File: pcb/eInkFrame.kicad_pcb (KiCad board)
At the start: 2 copper layers, 191.8 x 127.7 mm, 22 parts, among them J1 Socket Raspberry, J2 Socket IT8951, J3 Socket BME680, J40 Socket MPR121 comm, J41 Socket MPR121 contacts, U1 Raspberry, U2 IT8951_Driver, U3 CJMCU-680, U4 MPR121

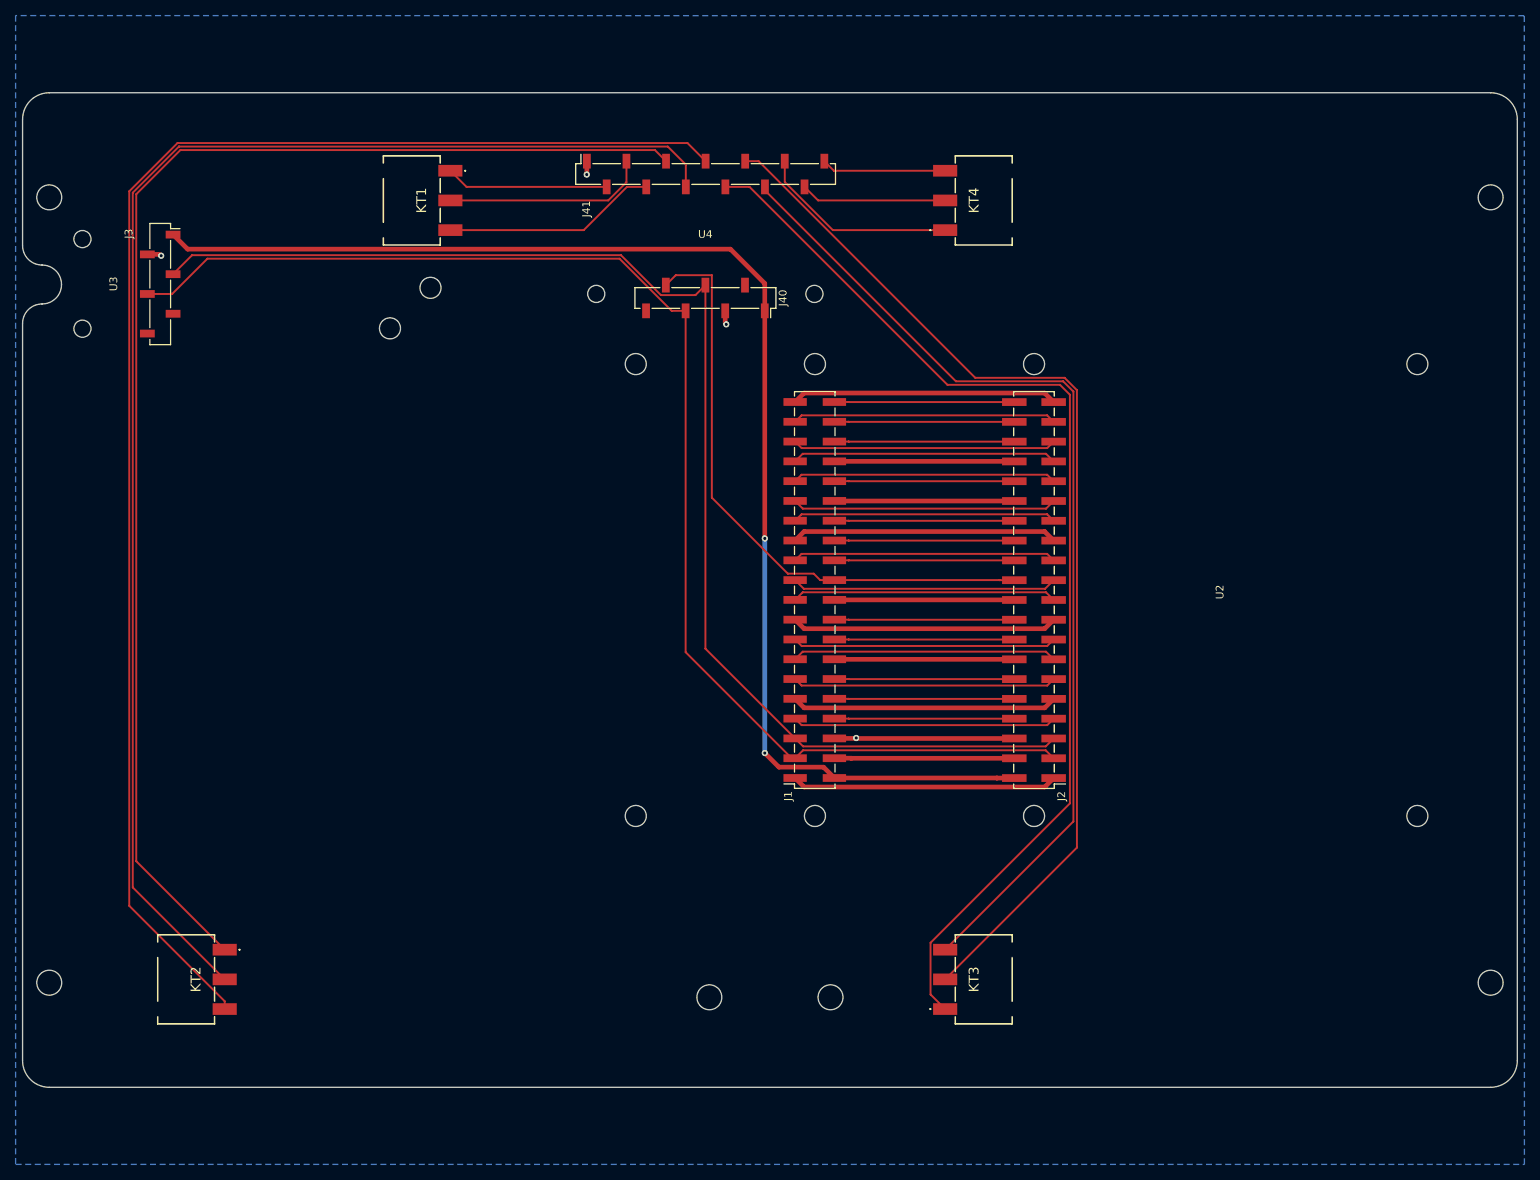
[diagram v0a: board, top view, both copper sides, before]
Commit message: Global doc cleanup, pcb and scripts enhancement, adding images
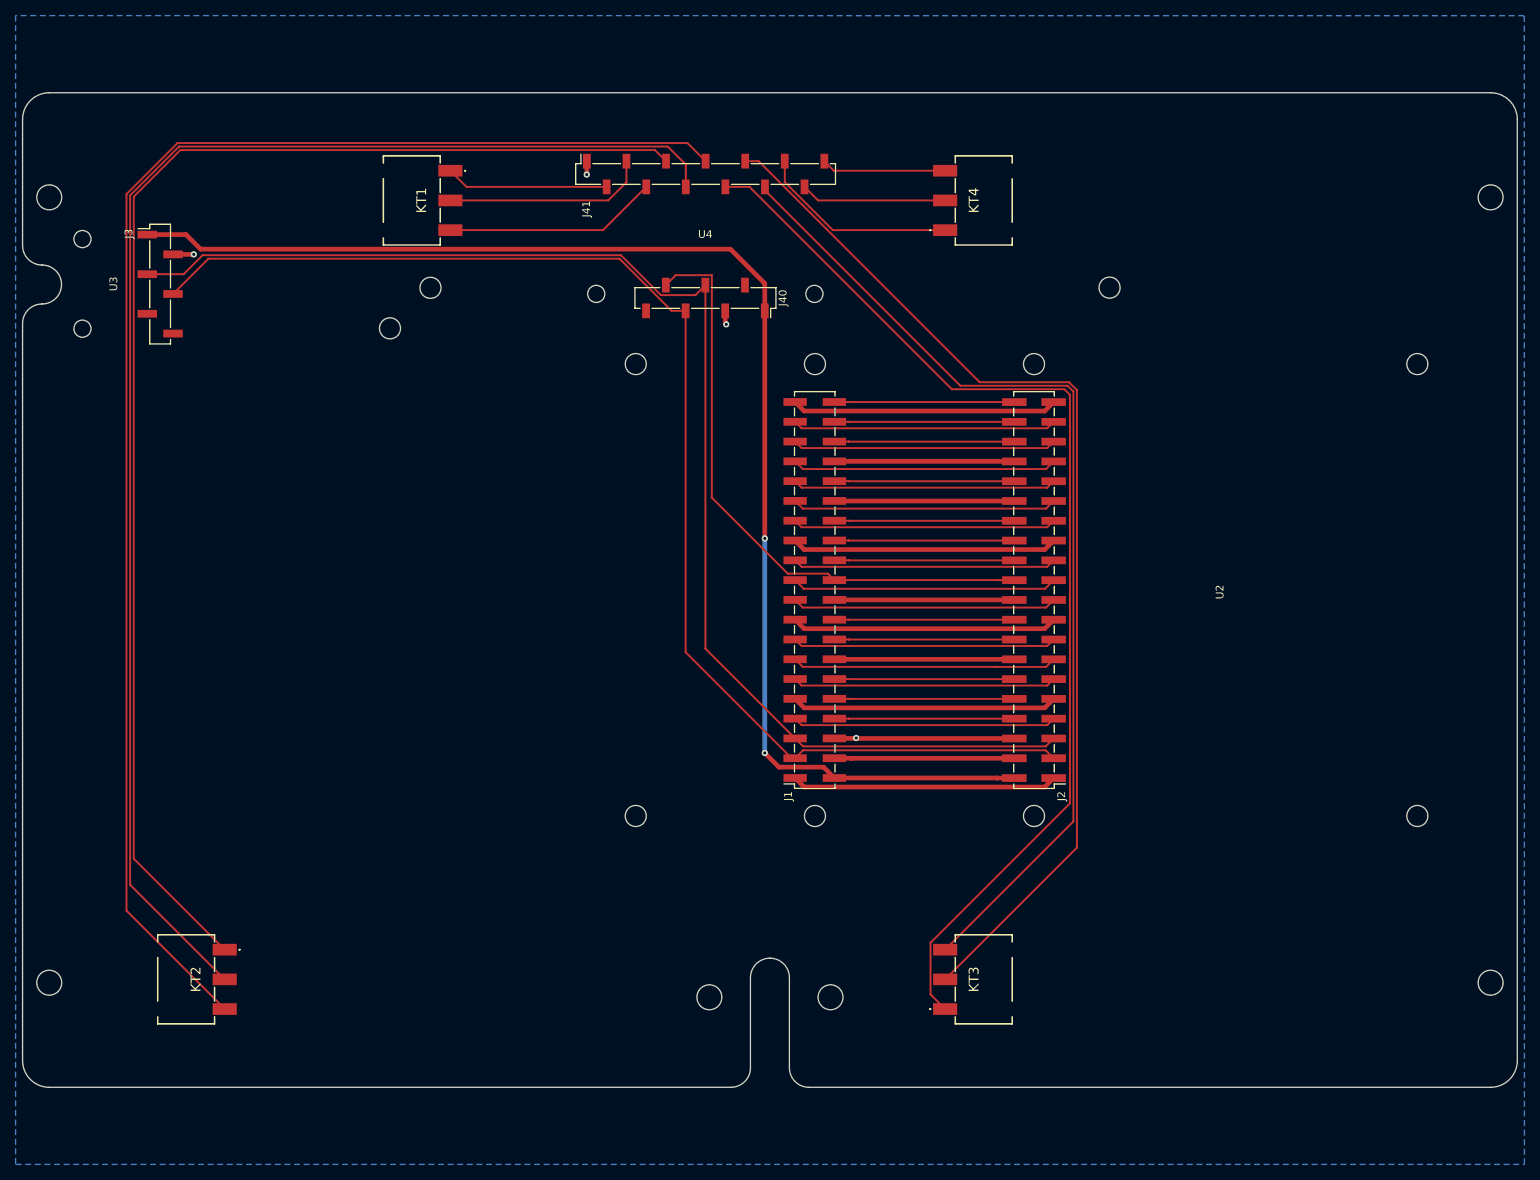
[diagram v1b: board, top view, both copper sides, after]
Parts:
- added HF3: M2.5, MountingHole:MountingHole_2.7mm_M2.5, F.Cu at (155.8, 50.9)
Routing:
- net VIN: track 172.2 -> 175.5 mm
- net SCL: track 169.0 -> 172.3 mm
- net SDA: track 171.3 -> 168.0 mm
- net GND: track 28.3 -> 29.3 mm
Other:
- outline, holes or cut-outs redrawn

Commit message: Change a hard to source component and adapt PCB accordingly + hide some Spotify elements + global formatting
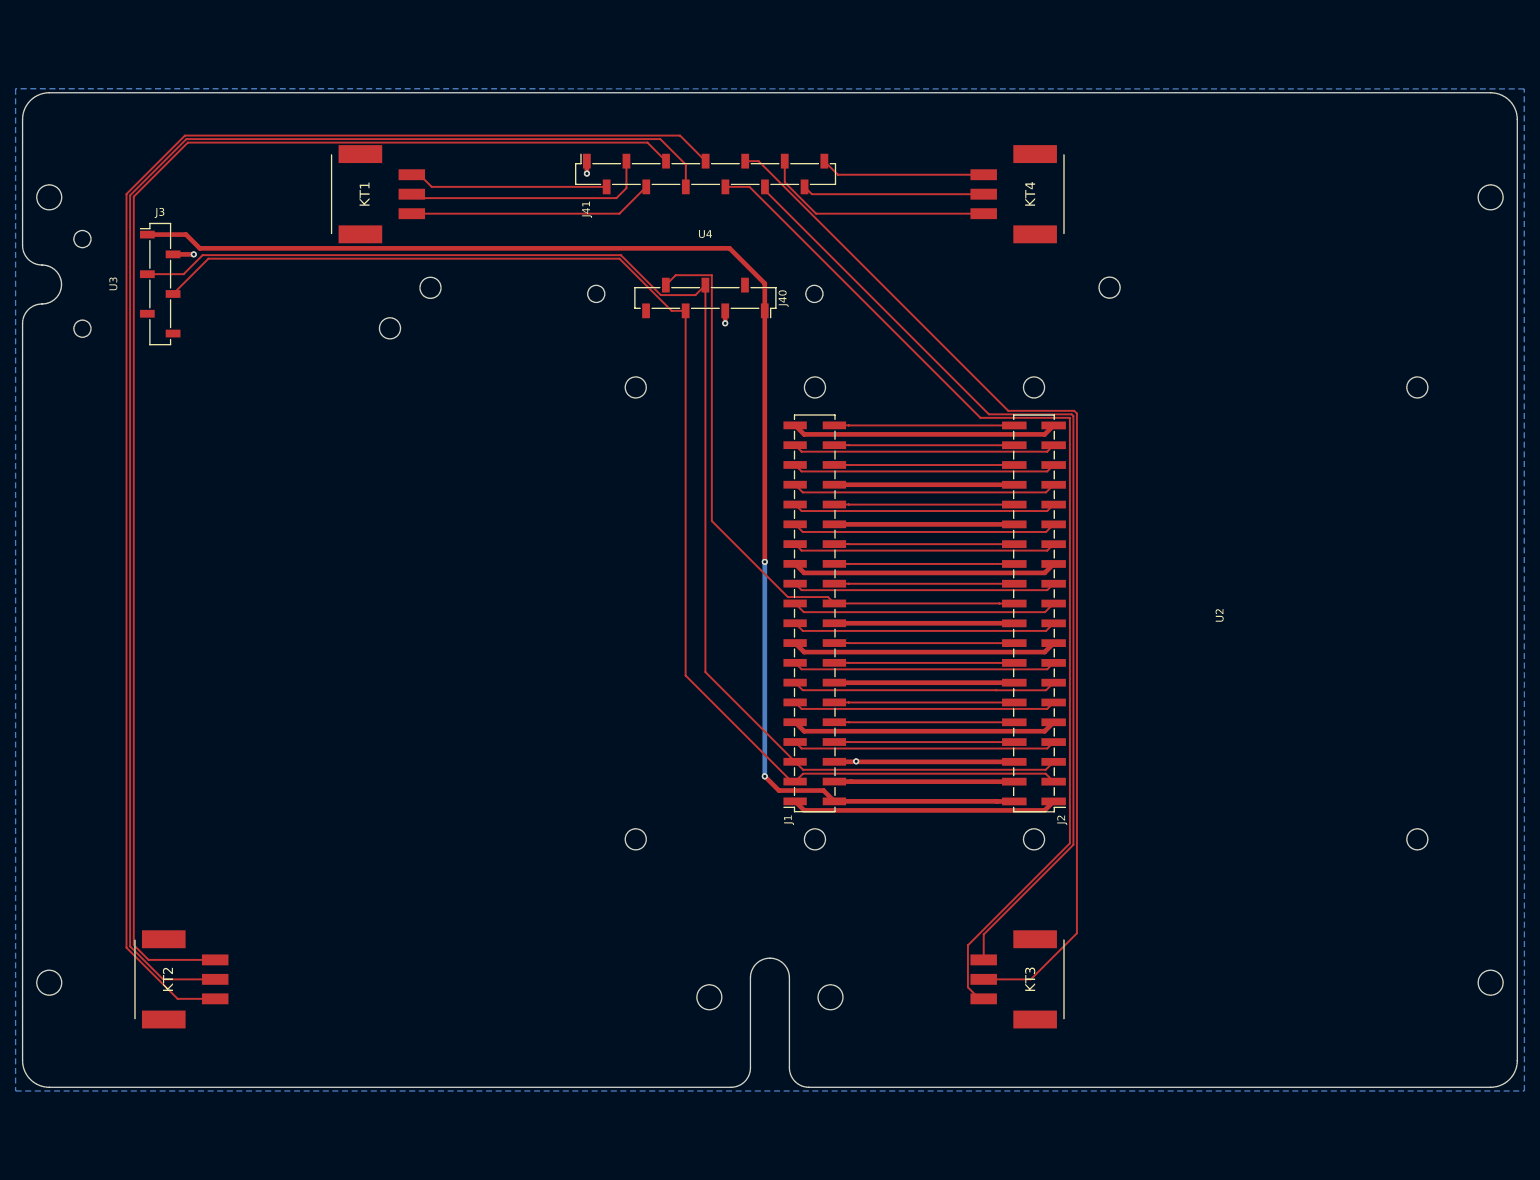
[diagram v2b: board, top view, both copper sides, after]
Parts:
- J3: footprint Connector_PinSocket_2.54mm:PinSocket_1x06_P2.54mm_Vertical_SMD_Pin1Right -> Connector_PinSocket_2.54mm:PinSocket_1x06_P2.54mm_Vertical_SMD_Pin1Left
- KT1, KT2, KT3, KT4: footprint eInkFrame:TE 2383945-3 (without clip) -> eInkFrame:Phoenix contact 1814647
- moved KT2 3.73 mm to (41.0, 139.7)
- moved J1 3.00 mm to (118.0, 92.7)
- moved J2 3.00 mm to (146.1, 92.7)
- moved U1 3.00 mm to (106.5, 92.7)
- moved U2 3.00 mm to (170.7, 92.7)
- moved KT1 0.80 mm to (66.2, 38.9)
- moved KT4 0.80 mm to (139.6, 38.9)
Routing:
- net Net-(J41-Pad5): track 172.9 -> 179.5 mm
- net Net-(J41-Pad3): track 26.3 -> 31.8 mm
- net Net-(J41-Pad13): track 16.0 -> 21.2 mm
- net Net-(J41-Pad2): track 20.9 -> 25.7 mm
- net Net-(J41-Pad8): track 142.3 -> 137.6 mm
- net Net-(J41-Pad12): track 18.8 -> 23.4 mm
- net Net-(J41-Pad6): track 183.4 -> 187.6 mm
- net Net-(J41-Pad11): track 25.8 -> 29.9 mm
- net Net-(J41-Pad4): track 27.4 -> 31.5 mm
- net SDA: track 168.0 -> 171.0 mm
- net SCL: track 172.3 -> 175.3 mm
- net MPR121_INT: track 78.2 -> 81.2 mm
- net VIN: track 175.5 -> 178.5 mm
- net Net-(J41-Pad10): track 129.2 -> 126.6 mm
- net Net-(J41-Pad7): track 187.8 -> 189.6 mm

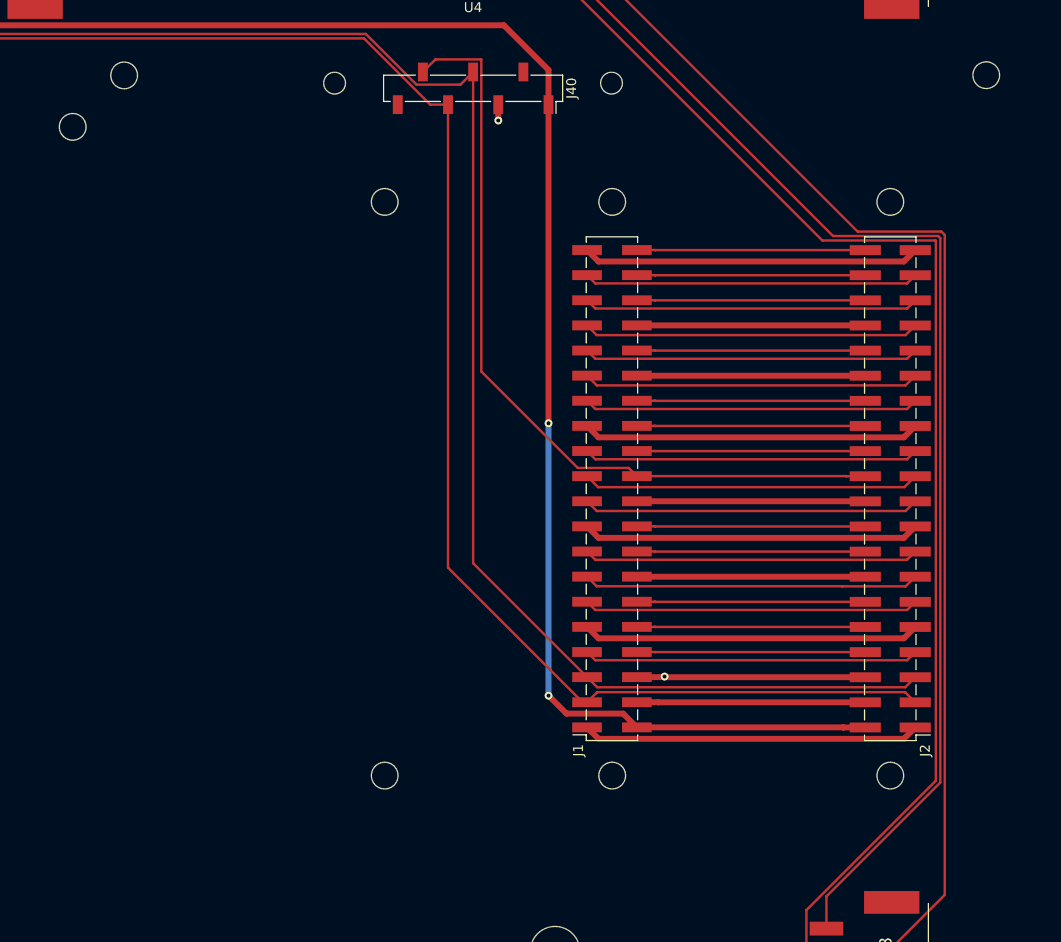
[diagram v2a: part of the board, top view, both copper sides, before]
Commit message: New PCB stand, adding photos, minor updates after final mounting
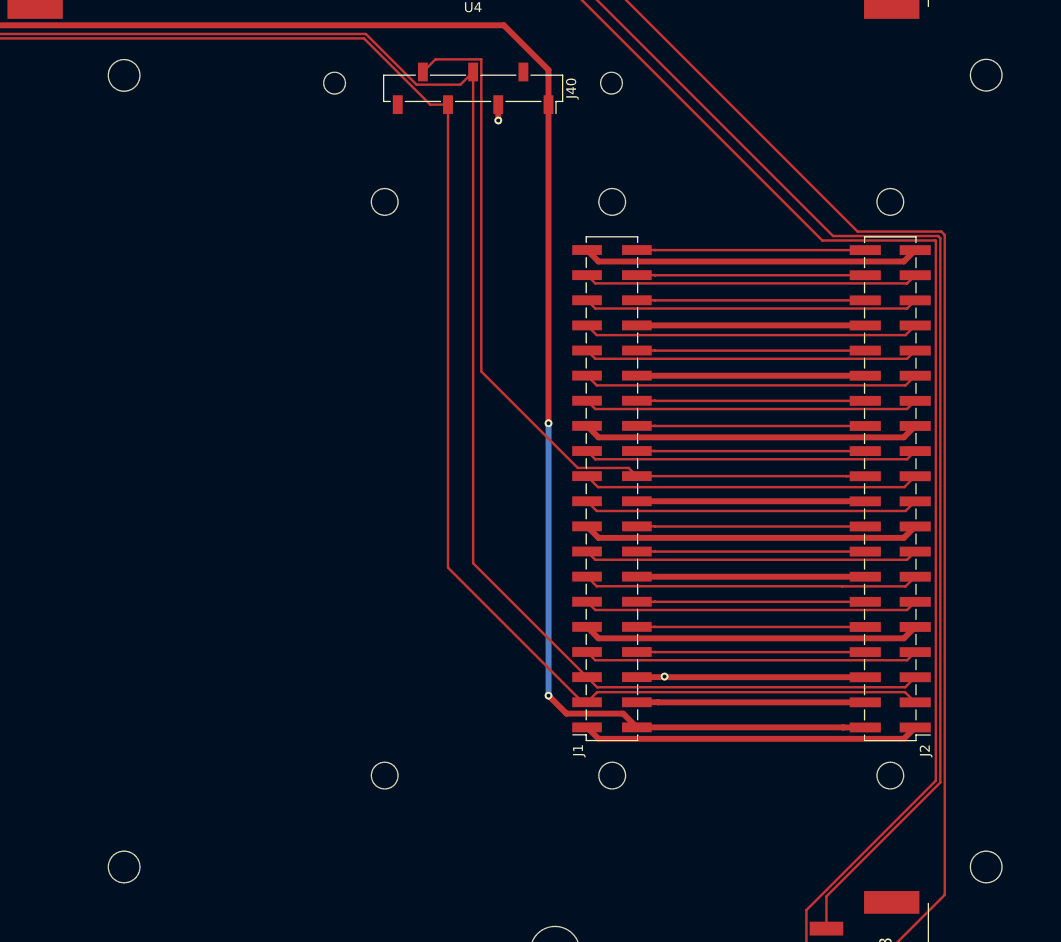
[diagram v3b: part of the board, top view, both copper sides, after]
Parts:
- added HF1: M3, MountingHole:MountingHole_3.2mm_M3, F.Cu at (68.6, 131.0)
- HF2: value M2.5 -> M3; footprint MountingHole:MountingHole_2.7mm_M2.5 -> MountingHole:MountingHole_3.2mm_M3
- HF3: renamed from HF1; value M2.5 -> M3; footprint MountingHole:MountingHole_2.7mm_M2.5 -> MountingHole:MountingHole_3.2mm_M3
- HF4: renamed from HF3; value M2.5 -> M3; footprint MountingHole:MountingHole_2.7mm_M2.5 -> MountingHole:MountingHole_3.2mm_M3
- KT1, KT2, KT3, KT4: value Screw_Terminal_01x03 -> Terminal_01x03
- moved HF2 118.9 mm to (155.8, 131.0), turned to 0 degrees
